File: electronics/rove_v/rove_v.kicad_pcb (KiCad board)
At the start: 2 copper layers, 60 x 50 mm, 32 parts, among them J1 USB-C, J2 Battery, J3 LeftMotor, J4 RightMotor, SW1 BOOT, U1 ESP32-S3-WROOM-1, U2 DRV8833PW, U3 XC6220B331MR, U4 TP4056

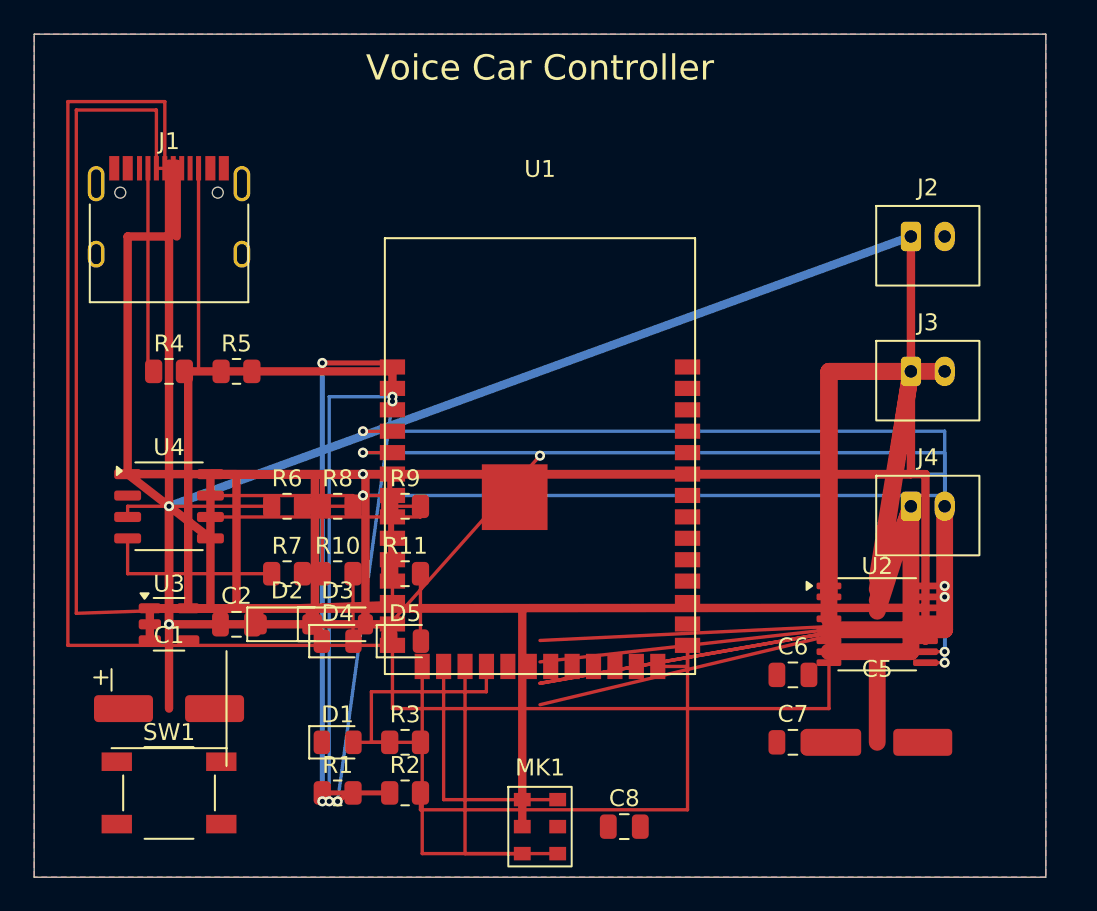
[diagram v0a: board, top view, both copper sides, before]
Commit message: Add ROVE-V completed PCB, docs, tools, and Gerbers
- PCB resized 100×80mm → 60×50mm (62% area reduction)
- Fully routed with freerouting, all DRC violations fixed manually
- DRU custom rules: JLCPCB 0.127mm min clearance + J1 USB-C override
- Final DRC: 145 violations (all J1 connector geometry), 0 unconnected
- Gerbers generated and ready for JLCPCB (rove_v_gerbers_drc_clean.zip)
- board_specs.md: ROVE-V section corrected (DW01A+FS8205A, no TP4056)
- tools/: export_dsn.py, import_ses.py, resize_board_60x50.py, etc.

Co-Authored-By: Claude Sonnet 4.6 <noreply@anthropic.com>
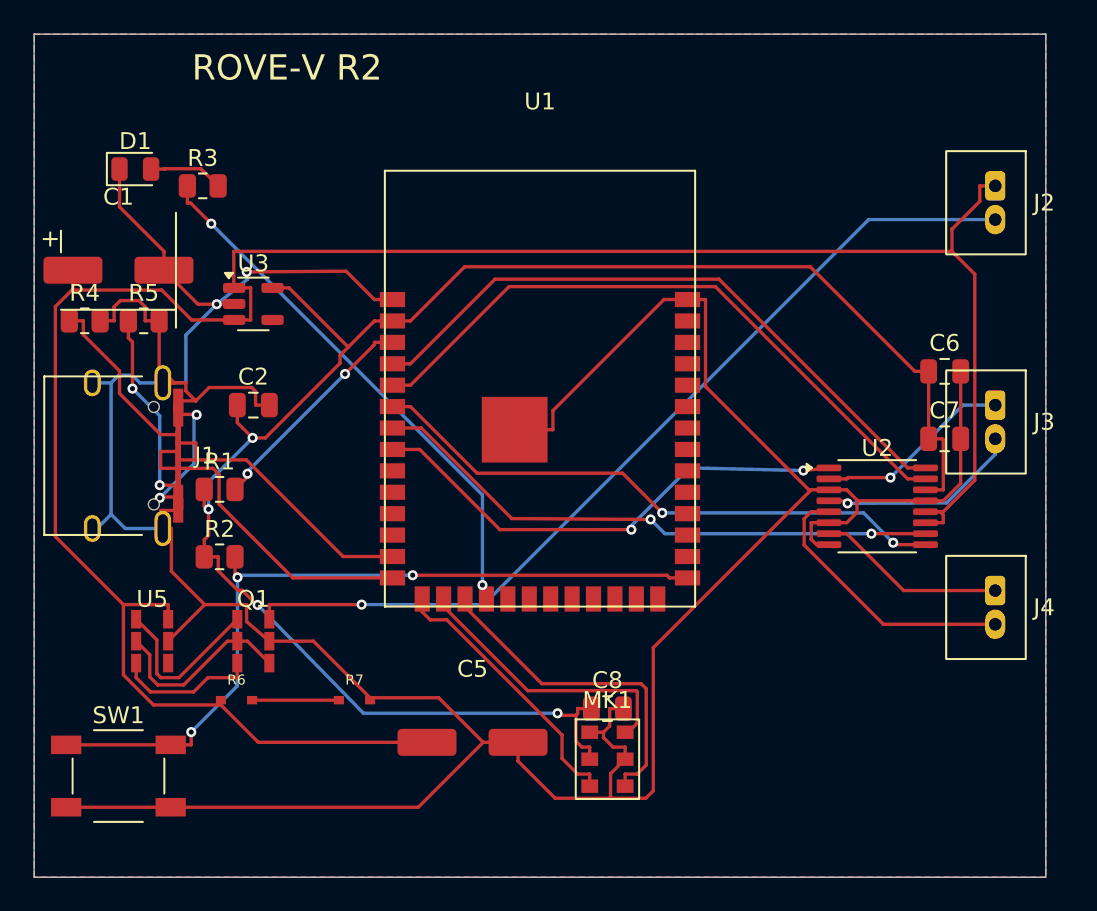
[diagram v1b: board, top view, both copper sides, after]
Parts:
- removed D2, D3: SS14, D_SOD-123
- removed D4: Red, LED_0805_2012Metric
- removed D5: Green, LED_0805_2012Metric
- removed R10, R11: 330R, R_0805_2012Metric
- removed R8, R9: 10k, R_0805_2012Metric
- removed U4: TP4056, SOP-8_3.9x4.9mm_P1.27mm
- added Q1: FS8205A, Package_TO_SOT_SMD:SOT-23-6, F.Cu at (13.0, 36.0)
- added U5: DW01A, Package_TO_SOT_SMD:SOT-23-6, F.Cu at (7.00, 36.0)
- R6: value 2k -> 100k; footprint R_0805_2012Metric -> Resistor_SMD:R_0402_1005Metric
- R7: value 10k -> 47k; footprint R_0805_2012Metric -> Resistor_SMD:R_0402_1005Metric
- moved D1 36.1 mm to (6.00, 8.00)
- moved R3 35.1 mm to (10.0, 9.00)
- moved C1 26.2 mm to (5.00, 14.0)
- moved C5 24.0 mm to (26.0, 42.0)
- moved C6 20.1 mm to (54.0, 20.0)
- moved C7 20.1 mm to (54.0, 24.0)
- moved U3 19.6 mm to (13.0, 16.0)
- moved R1 19.3 mm to (11.0, 27.0)
- moved R2 17.8 mm to (11.0, 31.0)
- moved J1 13.5 mm to (4.50, 25.0), turned to 270 degrees
- moved C2 13.0 mm to (13.0, 22.0)
- moved R6 11.9 mm to (12.0, 39.5)
- moved R7 8.50 mm to (19.0, 39.5)
- moved C8 7.07 mm to (34.0, 40.0)
- moved J4 7.07 mm to (57.0, 33.0), turned to 270 degrees
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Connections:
- J2 pad 2: GND -> /BATT_NEG
- R6 pad 1: /TP_PROG -> /VBAT
- R6 pad 2: GND -> /VBAT_MON
- R7 pad 1: /TP_TEMP -> /VBAT_MON
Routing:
- net GND: track 5.00 -> 219.0 mm, vias 1 -> 2
- net /3V3: track 190.3 -> 104.9 mm, vias 3 -> 4
- net /USB_5V: track 86.7 -> 8.05 mm, vias 0 -> 2
- net /VBAT: track 197.4 -> 133.6 mm, vias 1 -> 0
- net /BATT_NEG: track 0.00 -> 53.4 mm, vias 0 -> 1
- net /USB_D+: track 62.2 -> 19.5 mm
- net /EN: track 55.5 -> 13.2 mm, vias 4 -> 2
- net /USB_D-: track 59.1 -> 17.1 mm
- net /DRV_SLEEP: track 64.6 -> 29.5 mm, vias 0 -> 2
- net /RIGHT_IN1: track 68.9 -> 35.0 mm
- net /RIGHT_IN2: track 66.8 -> 34.2 mm
- net /LEFT_IN1: track 66.9 -> 38.3 mm, vias 2 -> 0
- net /LEFT_IN2: track 66.5 -> 38.8 mm, vias 2 -> 0
- net /AOUT2: track 34.6 -> 12.1 mm, vias 0 -> 1
- net /STATUS_LED: track 12.4 -> 32.0 mm, vias 0 -> 2
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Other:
- board text added: "ROVE-V R2"
- board text removed: "Voice Car Controller"
